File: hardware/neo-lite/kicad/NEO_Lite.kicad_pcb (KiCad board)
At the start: 2 copper layers, 56 x 72 mm, 47 parts, among them J1 USB-C, J2 OLED, J3 MIC INMP441, J4 ALTAVOZ 8 Ω, J5 EXPANSIÓN, Q1 MMBT3904, Q2 MMBT3904, SW1 RESET, SW2 BOOT, U1 TLV1117LV33, U2 ESP32-S3-WROOM-1-N16R8, U3 CH340C, U4 MAX98357A

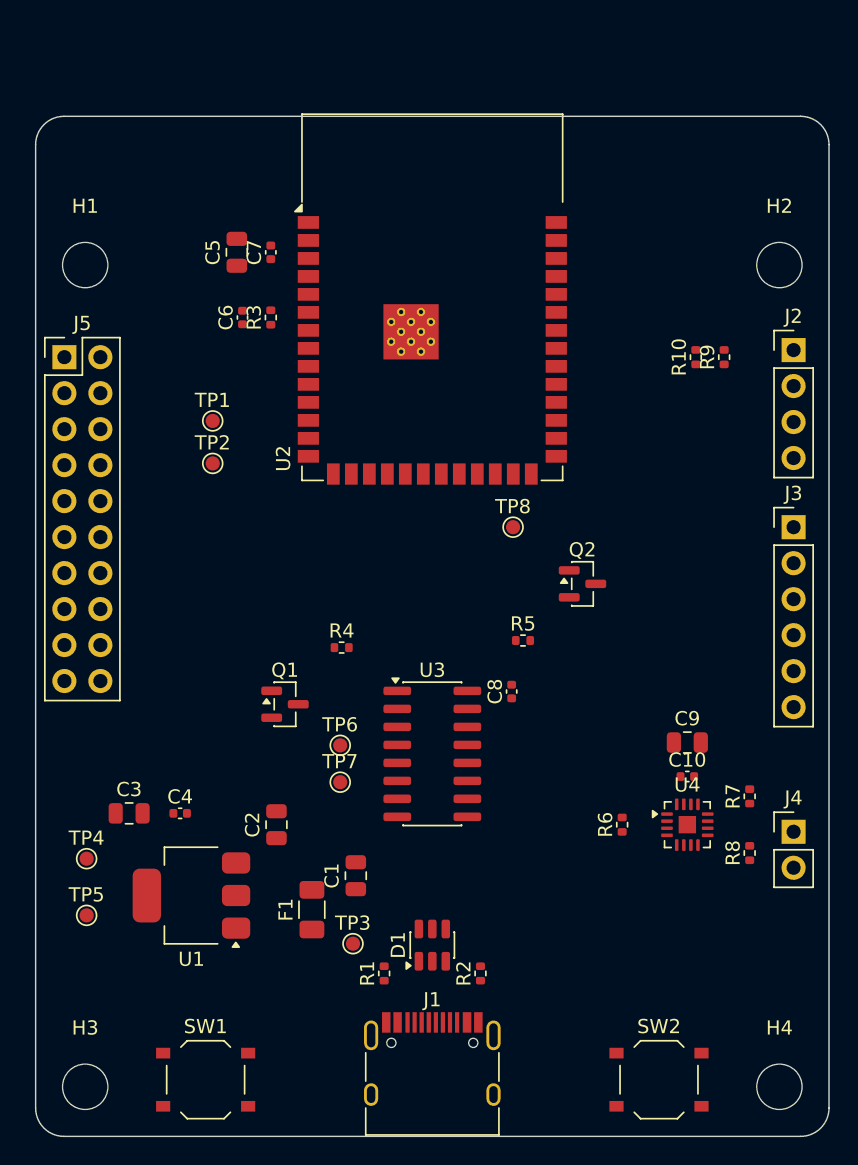
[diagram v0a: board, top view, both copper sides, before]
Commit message: hardware(neo-lite): revisión B compacta, WROOM-1U y USB nativo
Módulo ESP32-S3-WROOM-1U-N16R8 (mismas capacidades, antena externa por
U.FL), USB nativo del S3 en lugar del CH340C y el autorreset, sin la tira
de expansión J5. Placa de 31 x 43 mm (antes 56 x 72), DRC sin errores
salvo lo no ruteado; coste estimado de 72,33 USD por 5 placas.

Co-Authored-By: Claude Opus 5.5 <noreply@anthropic.com>
Claude-Session: https://claude.ai/code/session_01T89H8KVmFbTbbN7gPJgPo2
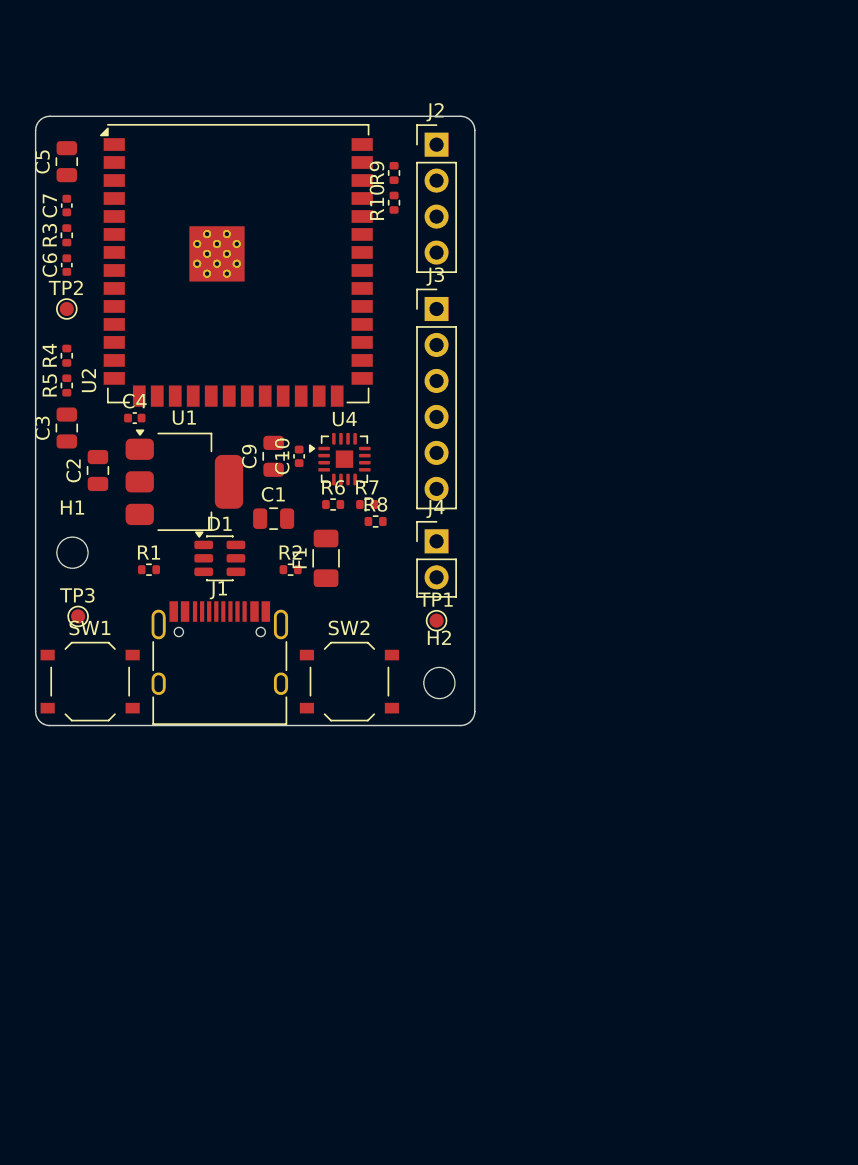
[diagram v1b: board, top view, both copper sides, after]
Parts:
- removed C8: 100nF, Capacitor_SMD:C_0402_1005Metric
- removed H3, H4: M3, MountingHole:MountingHole_3.2mm_M3
- removed J5: EXPANSIÓN, Connector_PinHeader_2.54mm:PinHeader_2x10_P2.54mm_Vertical
- removed Q1, Q2: MMBT3904, Package_TO_SOT_SMD:SOT-23
- removed TP4: +3V3, TestPoint:TestPoint_Pad_D1.0mm
- removed TP5: GND, TestPoint:TestPoint_Pad_D1.0mm
- removed TP6: U0TXD, TestPoint:TestPoint_Pad_D1.0mm
- removed TP7: U0RXD, TestPoint:TestPoint_Pad_D1.0mm
- removed TP8: GPIO48, TestPoint:TestPoint_Pad_D1.0mm
- removed U3: CH340C, Package_SO:SOIC-16_3.9x9.9mm_P1.27mm
- H1, H2: value M3 -> M2; footprint MountingHole:MountingHole_3.2mm_M3 -> MountingHole:MountingHole_2.2mm_M2
- R4, R5: value 10k -> 22
- TP1: value USB_NAT_DP -> +5V
- TP2: value USB_NAT_DN -> +3V3
- TP3: value +5V -> GND
- U2: value ESP32-S3-WROOM-1-N16R8 -> ESP32-S3-WROOM-1U-N16R8; footprint RF_Module:ESP32-S3-WROOM-1 -> RF_Module:ESP32-S3-WROOM-1U
- moved H2 38.0 mm to (128.5, 140.0)
- moved R5 36.9 mm to (102.2, 119.0), turned to 90 degrees
- moved SW2 35.6 mm to (122.2, 139.9)
- moved C10 35.5 mm to (118.6, 124.0), turned to 90 degrees
- moved C9 35.5 mm to (116.8, 124.0), turned to 90 degrees
- moved U4 35.4 mm to (121.8, 124.2)
- moved R8 35.3 mm to (124.0, 128.6), turned to 0 degrees
- moved R7 34.0 mm to (123.4, 127.4), turned to 0 degrees
- moved R1 33.0 mm to (108.0, 132.0), turned to 0 degrees
- moved J1 32.6 mm to (113.0, 139.0)
- moved J4 32.5 mm to (128.3, 130.0)
- moved R2 31.5 mm to (118.0, 132.0), turned to 0 degrees
- moved D1 31.1 mm to (113.0, 131.2), turned to 0 degrees
- moved R6 30.4 mm to (121.0, 127.4), turned to 0 degrees
- moved TP3 30.2 mm to (103.0, 135.3)
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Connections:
- R4 pad 1: /DTR -> /USB_DP
- R4 pad 2: /Q1_B -> /ESP_DP
- R5 pad 1: /RTS -> /USB_DN
- R5 pad 2: /Q2_B -> /ESP_DN
- TP1 pad 1: /USB_NAT_DP -> +5V
- TP2 pad 1: /USB_NAT_DN -> +3V3
- TP3 pad 1: +5V -> GND
- U2 pad 10: /GPIO17 -> unconnected-(U2-IO17-Pad10)
- U2 pad 11: /GPIO18 -> unconnected-(U2-IO18-Pad11)
- U2 pad 12: /GPIO8 -> unconnected-(U2-IO8-Pad12)
- U2 pad 13: /USB_NAT_DN -> /ESP_DN
- U2 pad 14: /USB_NAT_DP -> /ESP_DP
- U2 pad 17: /GPIO9 -> unconnected-(U2-IO9-Pad17)
- U2 pad 18: /GPIO10 -> unconnected-(U2-IO10-Pad18)
- U2 pad 19: /GPIO11 -> unconnected-(U2-IO11-Pad19)
- U2 pad 20: /GPIO12 -> unconnected-(U2-IO12-Pad20)
- U2 pad 21: /GPIO13 -> unconnected-(U2-IO13-Pad21)
- U2 pad 25: /GPIO48 -> unconnected-(U2-IO48-Pad25)
- U2 pad 31: /GPIO38 -> unconnected-(U2-IO38-Pad31)
- U2 pad 32: /GPIO39 -> unconnected-(U2-IO39-Pad32)
- U2 pad 36: /U0RXD -> unconnected-(U2-RXD0-Pad36)
- U2 pad 37: /U0TXD -> unconnected-(U2-TXD0-Pad37)
- U2 pad 4: /GPIO4 -> unconnected-(U2-IO4-Pad4)
- U2 pad 5: /GPIO5 -> unconnected-(U2-IO5-Pad5)
- U2 pad 6: /GPIO6 -> unconnected-(U2-IO6-Pad6)
- U2 pad 7: /GPIO7 -> unconnected-(U2-IO7-Pad7)
- U2 pad 8: /GPIO15 -> unconnected-(U2-IO15-Pad8)
- U2 pad 9: /GPIO16 -> unconnected-(U2-IO16-Pad9)
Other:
- board size 56 x 72 mm -> 31 x 43 mm

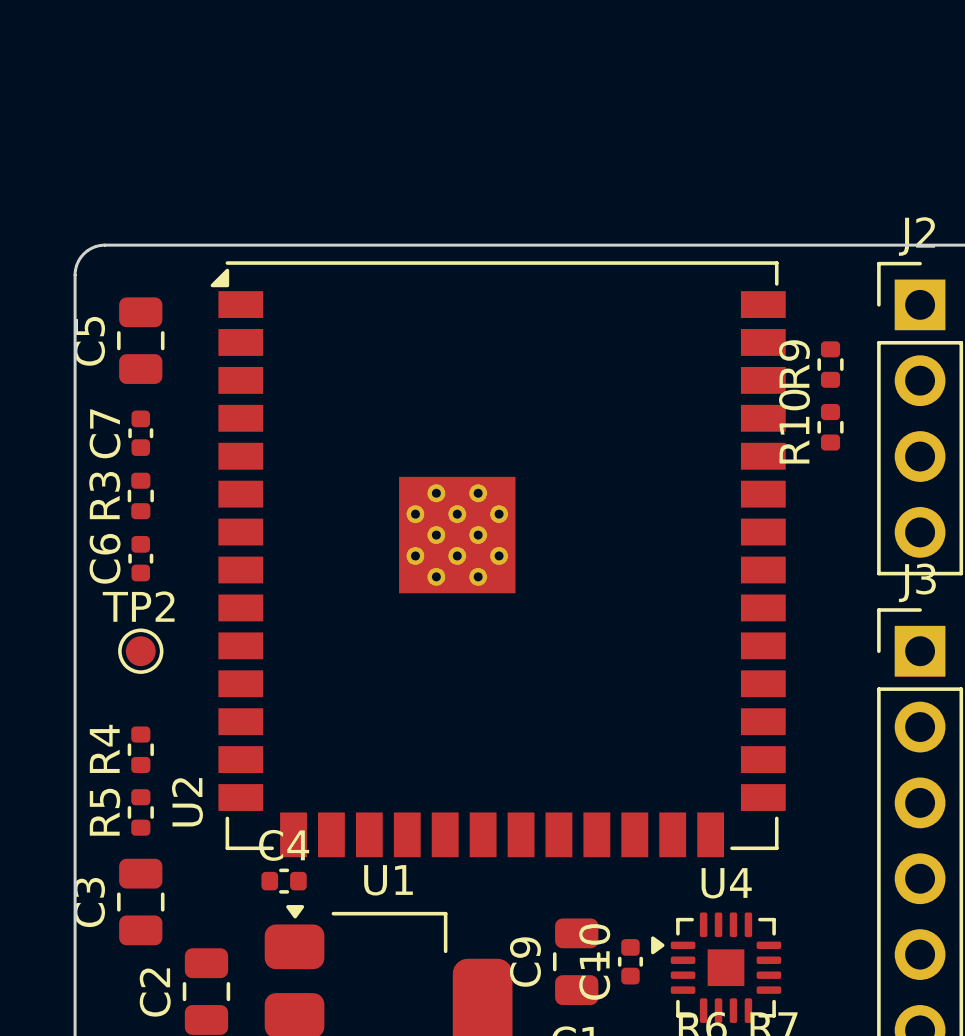
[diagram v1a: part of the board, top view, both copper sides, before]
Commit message: hardware(neo-lite): WROOM-1 con la antena fuera del borde en lugar del 1U
El usuario descarta la antena externa del WROOM-1U. Se vuelve al
ESP32-S3-WROOM-1-N16R8 con antena integrada, colocado con la antena
sobresaliendo del borde superior (posición recomendada por Espressif).
La placa sigue en 31 x 43 mm, DRC sin errores salvo lo no ruteado;
coste estimado de 73,14 USD por 5 placas.

Co-Authored-By: Claude Opus 5.5 <noreply@anthropic.com>
Claude-Session: https://claude.ai/code/session_01T89H8KVmFbTbbN7gPJgPo2
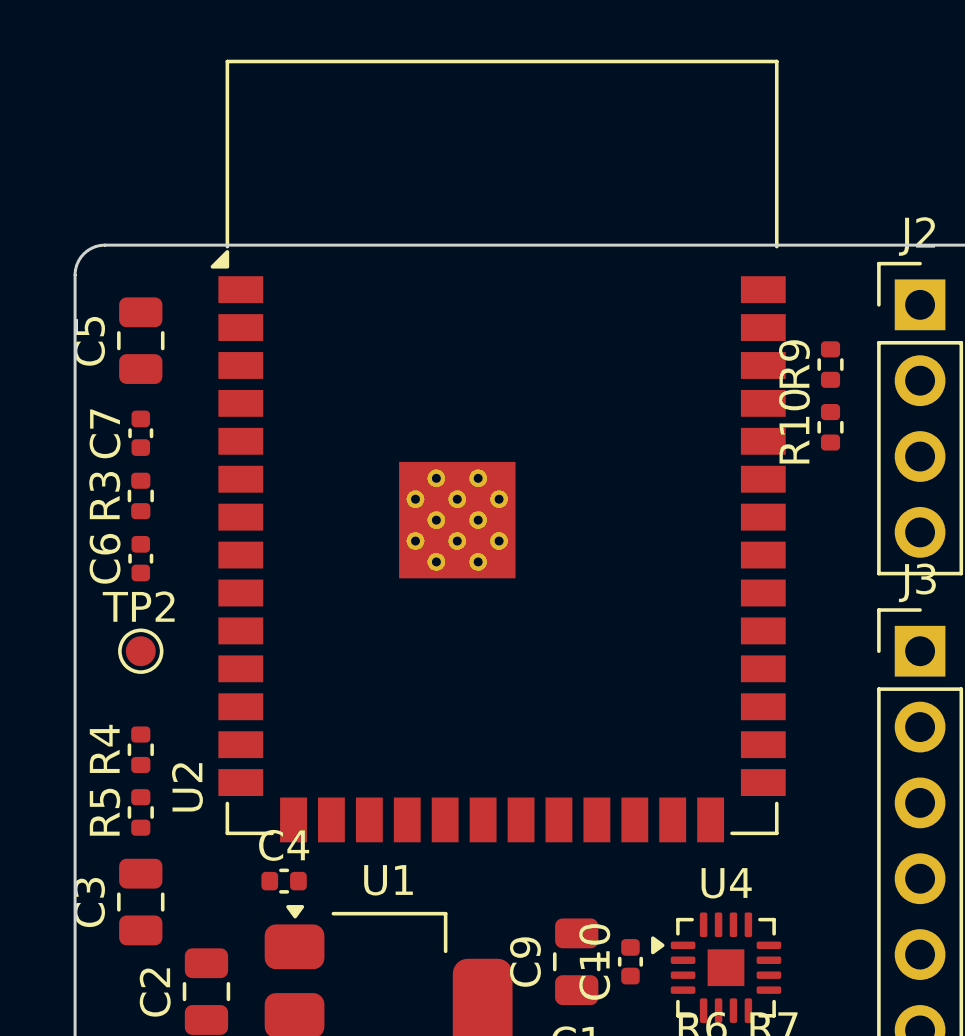
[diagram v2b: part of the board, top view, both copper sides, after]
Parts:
- U2: value ESP32-S3-WROOM-1U-N16R8 -> ESP32-S3-WROOM-1-N16R8; footprint RF_Module:ESP32-S3-WROOM-1U -> RF_Module:ESP32-S3-WROOM-1
- moved U2 3.65 mm to (114.3, 106.8)

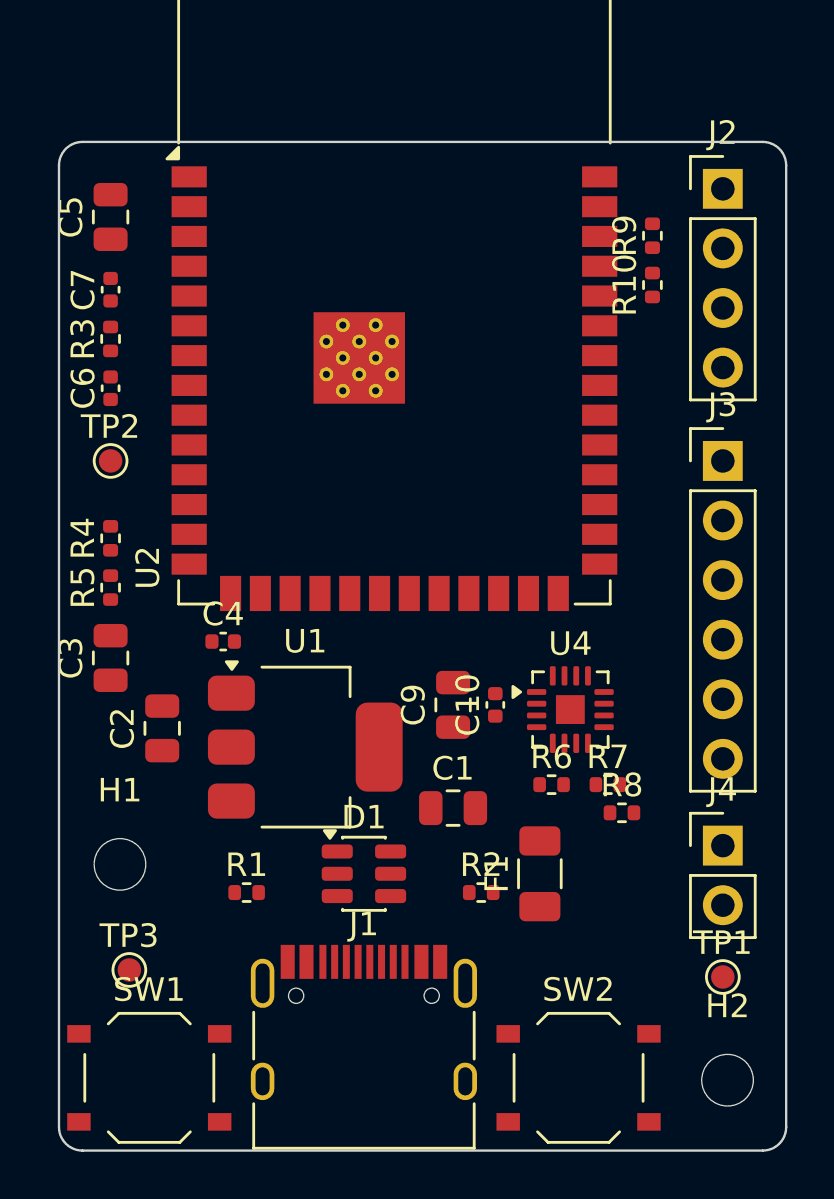
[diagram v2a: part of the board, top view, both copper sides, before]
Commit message: hardware(neo-lite): fase 4, ruteo completo y DRC limpio
PCB de 31 x 43 mm ruteada con Freerouting 2.1 y planos de GND en las dos
caras con cosido. DRC sin conexiones pendientes ni errores de cobre y
sin diferencias con el esquemático; 716 mm de pista y 81 vías.

Co-Authored-By: Claude Opus 5.5 <noreply@anthropic.com>
Claude-Session: https://claude.ai/code/session_01T89H8KVmFbTbbN7gPJgPo2
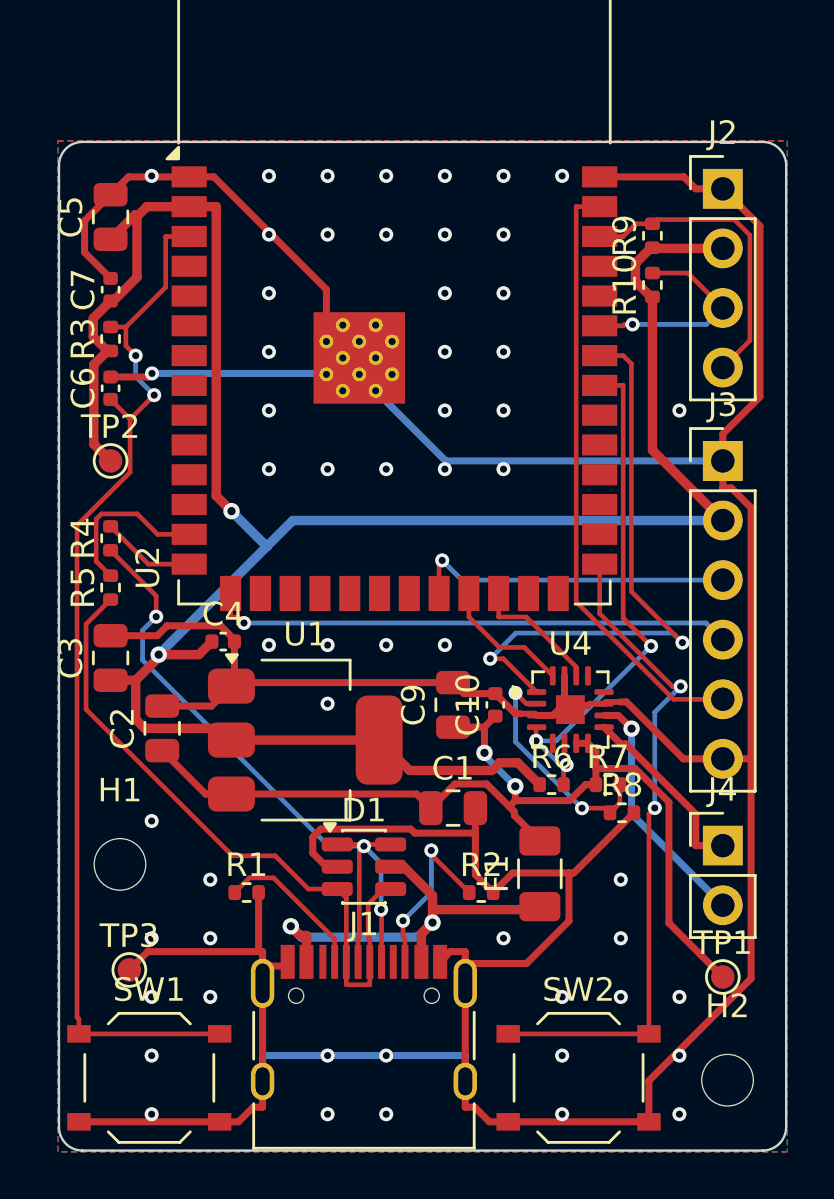
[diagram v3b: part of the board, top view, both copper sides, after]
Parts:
- moved U1 0.30 mm to (110.5, 125.5)
- moved D1 0.30 mm to (113.0, 130.9)
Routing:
- net GND: track 0.00 -> 222.4 mm, vias 0 -> 55
- net +3V3: track 0.00 -> 101.1 mm, vias 0 -> 2
- net /EN: track 0.00 -> 45.4 mm, vias 0 -> 2
- net +5V: track 0.00 -> 42.9 mm, vias 0 -> 2
- net /USB_DP: track 0.00 -> 31.1 mm, vias 0 -> 3
- net /USB_DN: track 0.00 -> 28.9 mm
- net /BOOT: track 0.00 -> 28.2 mm, vias 0 -> 2
- net /MIC_WS: track 0.00 -> 25.8 mm
- net /SPK_DIN: track 0.00 -> 25.7 mm, vias 0 -> 2
- net /AMP_SD: track 0.00 -> 22.4 mm, vias 0 -> 3
- net /MIC_SCK: track 0.00 -> 22.4 mm, vias 0 -> 1
- net VBUS: track 0.00 -> 18.4 mm, vias 0 -> 2
- net /MIC_SD: track 0.00 -> 13.8 mm, vias 0 -> 1
- net /I2C_SDA: track 0.00 -> 13.1 mm
- net /SPK_N: track 0.00 -> 10.5 mm, vias 0 -> 1
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- added copper zone on B.Cu, net GND
- added copper zone on F.Cu, net GND

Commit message: hardware(neo-lite): fase 5 en curso, serigrafía limpia y rotulada
Referencias a F.Fab y rótulos de banco: orden de pines de OLED, micrófono
y altavoz, RST/BOOT, tensiones de los puntos de prueba y nombre de la
placa. DRC sin avisos de serigrafía. Se añaden las herramientas de
comparación de huellas con EasyEDA de NEO v2.

Co-Authored-By: Claude Opus 5.5 <noreply@anthropic.com>
Claude-Session: https://claude.ai/code/session_01T89H8KVmFbTbbN7gPJgPo2
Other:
- board text added: "+"
- board text added: "-"
- board text added: "2026-10 techmiguel/neo-robot"
- board text added: "3V3"
- board text added: "5V"
- board text added: "BOOT"
- board text added: "GND"
- board text added: "L/R"
- board text added: "MIC"
- board text added: "NEO Lite rev B"
- board text added: "OLED"
- board text added: "RST"
- board text added: "SCK"
- board text added: "SCL"
- board text added: "SD"
- board text added: "SDA"
- board text added: "SPK"
- board text added: "WS"

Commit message: hardware(neo-lite): fase 6, revisión del PCB y revisión C lista para fabricar
Revisión exhaustiva del PCB en busca de errores de concepto y de ruteo que el
DRC no detecta, con todas las correcciones aplicadas:

- Enchufado en caliente: el LC cable-cerámicos podía llevar +5V a 7-8,5 V
  (máximo absoluto de U1 y U4: 6 V). C1 pasa a tántalo AVX TPS de 47 µF/16 V
  con ESR de 0,35 Ω (C444805); tools/hotplug_sim.py lo cuantifica.
- USB-C 0,35 mm hacia dentro del borde: ahora sobresale 0,25 mm.
- Par USB sin vías y en la cara superior, con D1 en flujo continuo y R4/R5
  en el recorrido (tools/preroute.py, pistas bloqueadas).
- Desacoplo junto a los pines (C7, C9, C10) y RC de EN junto al pin EN.
- U1 girado 180° con zona de +3V3 en la lengüeta (26 mm² + lengüeta).
- Sin pistas superiores bajo el módulo; islas del plano cosidas.
- Serigrafía con trazo de 0,15 mm.

tools/review_pcb.py codifica las comprobaciones (24/24 OK) y route_all.py
solo acepta ruteos que las pasan. DRC con paridad: 0 errores, 0 pendientes.
Documentado en docs/fase6-revision.md; fases 1, 2, 4 y 5 actualizadas.

Co-Authored-By: Claude Opus 5.5 <noreply@anthropic.com>
Claude-Session: https://claude.ai/code/session_01T89H8KVmFbTbbN7gPJgPo2
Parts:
- C1: value 10uF -> 47uF 16V; footprint Capacitor_SMD:C_0805_2012Metric -> Capacitor_Tantalum_SMD:CP_EIA-6032-28_Kemet-C
- moved C2 12.3 mm to (116.5, 123.0)
- moved R8 7.96 mm to (118.6, 122.8), turned to 180 degrees
- moved C9 7.50 mm to (122.6, 128.8), turned to 0 degrees
- moved C5 6.40 mm to (102.2, 109.6)
- moved R7 5.88 mm to (118.6, 124.0)
- moved C1 5.80 mm to (121.6, 131.7), turned to 180 degrees
- moved C6 5.75 mm to (102.2, 104.8)
- moved C4 5.73 mm to (105.4, 126.8), turned to -90 degrees
- moved C10 4.76 mm to (122.3, 127.0), turned to 0 degrees
- moved R4 4.70 mm to (104.1, 121.2)
- moved F1 4.34 mm to (121.6, 135.4), turned to 0 degrees
- moved C3 3.77 mm to (105.4, 124.0)
- moved C7 3.70 mm to (102.2, 102.6)
- moved R6 3.22 mm to (118.6, 125.2)
- moved R1 2.93 mm to (110.9, 131.6), turned to 90 degrees
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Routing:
- net GND: track 222.4 -> 111.0 mm, vias 55 -> 66
- net +3V3: track 101.1 -> 87.9 mm, vias 2 -> 5
- net /AMP_SD: track 22.4 -> 33.7 mm, vias 3 -> 2
- net /GAIN: track 9.96 -> 2.50 mm, vias 2 -> 0
- net /SPK_N: track 10.5 -> 17.1 mm, vias 1 -> 0
- net /BOOT: track 28.2 -> 34.1 mm, vias 2 -> 0
- net /MIC_WS: track 25.8 -> 31.1 mm, vias 0 -> 1
- net /MIC_SD: track 13.8 -> 18.8 mm, vias 1 -> 3
- net /USB_DP: track 31.1 -> 26.4 mm, vias 3 -> 0
- net /SPK_DIN: track 25.7 -> 21.1 mm
- net +5V: track 42.9 -> 47.0 mm, vias 2 -> 4
- net /CC2: track 7.75 -> 4.23 mm, vias 2 -> 0
- net /I2C_SCL: track 9.18 -> 12.6 mm
- net /USB_DN: track 28.9 -> 25.8 mm
- net /CC1: track 6.57 -> 3.85 mm
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- added copper zone on F.Cu, net +3V3
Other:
- board text added: "NEO Lite rev C"
- board text removed: "NEO Lite rev B"
